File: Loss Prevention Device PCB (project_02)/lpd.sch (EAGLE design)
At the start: 5 parts, among them K1 LPPB041NGCN-RC, U2 GT-U7, U3 HM-10

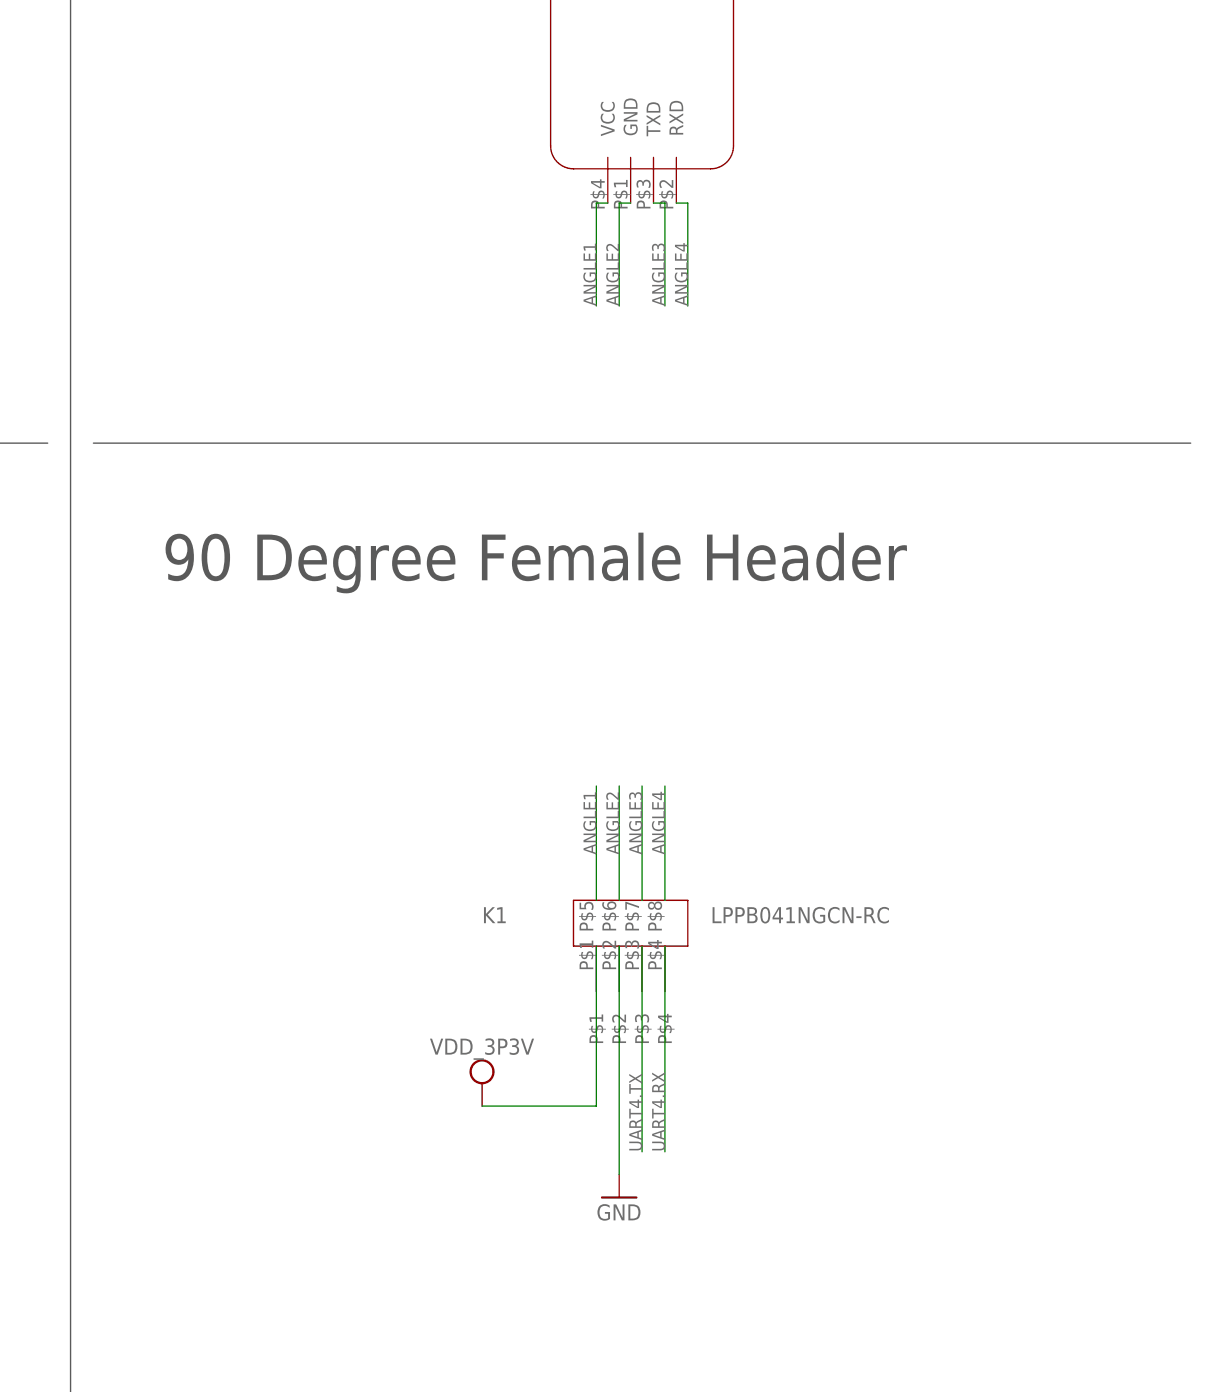
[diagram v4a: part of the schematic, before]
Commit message: Removed 90 degree header and updated footprints
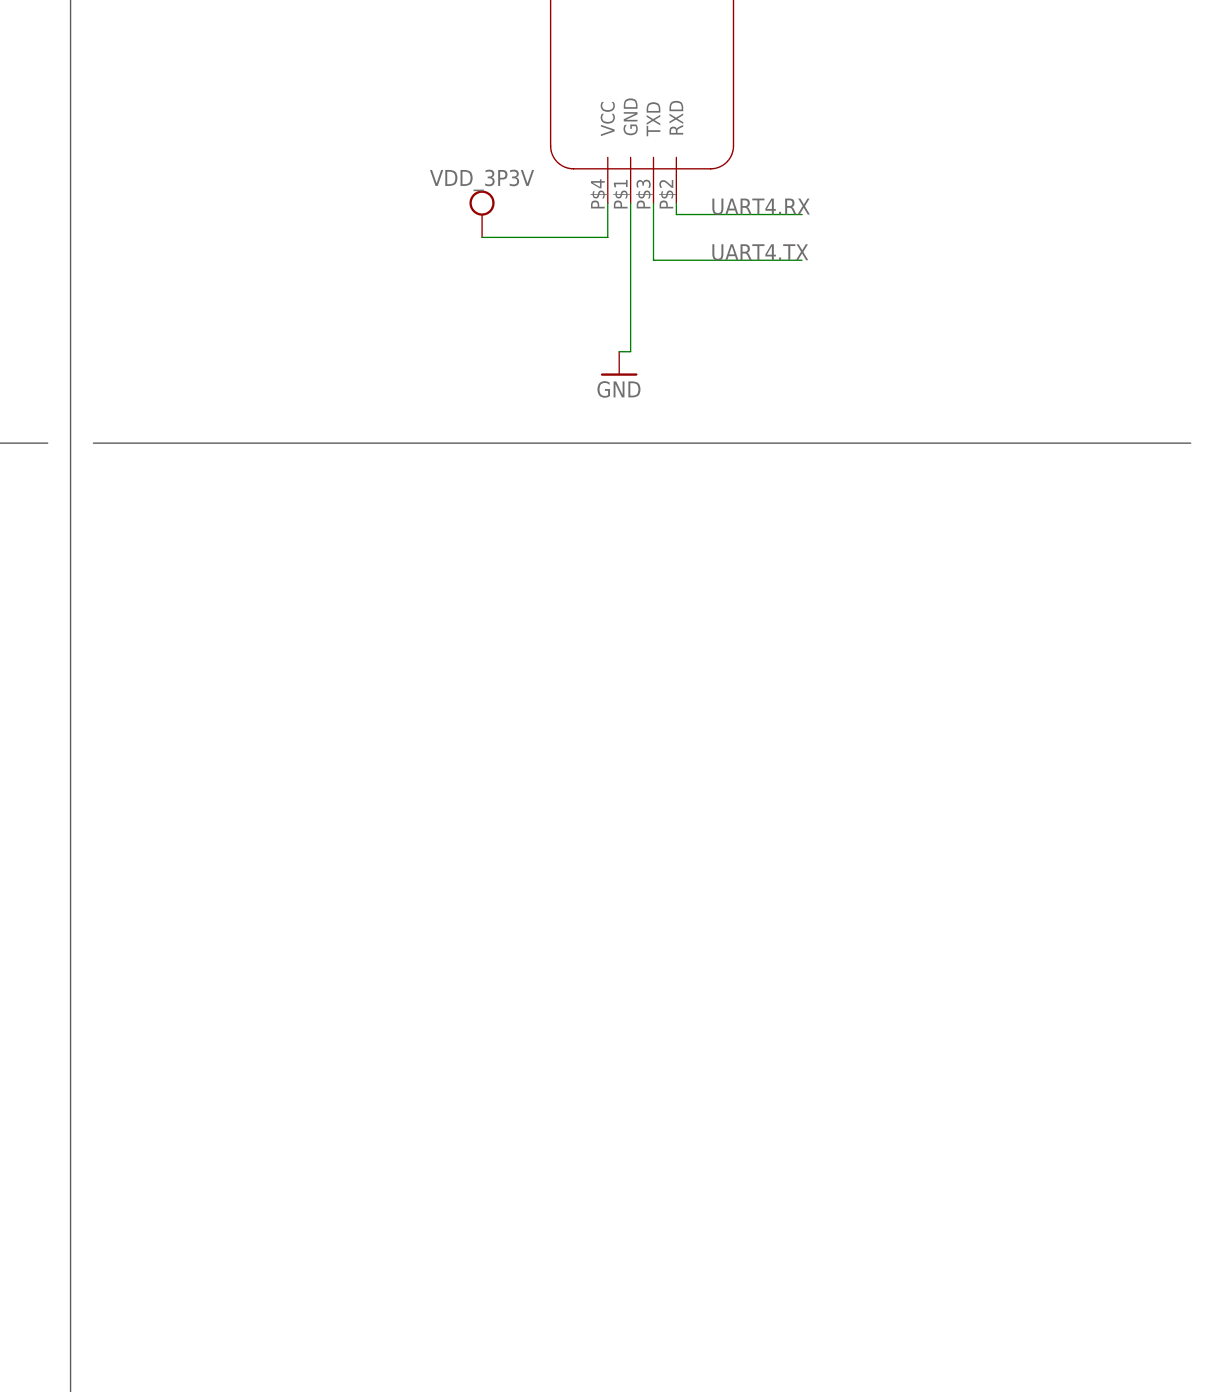
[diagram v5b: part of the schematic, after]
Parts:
- removed K1: LPPB041NGCN-RC, lpd:LPPB041NGCN-RC
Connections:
- removed net ANGLE1: K1.P$5, U3.VCC
- removed net ANGLE2: K1.P$6, U3.GND
- removed net ANGLE3: K1.P$7, U3.TXD
- removed net ANGLE4: K1.P$8, U3.RXD
- net GND: now also U3.GND; no longer K1.P$2
- net UART4.RX: now also U3.RXD; no longer K1.P$4
- net UART4.TX: now also U3.TXD; no longer K1.P$3
- net VDD_3P3V: now also U3.VCC; no longer K1.P$1
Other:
- note removed: "90 Degree Female Header"
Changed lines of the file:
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@@
 <parts>
 <part name="FRAME1" library="ENGI301" deviceset="FRAMES_A3L-LOC" device=""/>
-<part name="K1" library="lpd" deviceset="LPPB041NGCN-RC" device=""/>
 <part name="U2" library="lpd" deviceset="GT-U7" device=""/>
 <part name="X1" library="lpd" deviceset="GHI2_USB_HOST_W/CHASSIS_GND" device=""/>
@@
 <part name="SUPPLY3" library="lpd" deviceset="VDD_3P3V" device=""/>
 <part name="GND4" library="lpd" deviceset="GND" device=""/>
-<part name="GND5" library="lpd" deviceset="GND" device=""/>
-<part name="SUPPLY4" library="lpd" deviceset="VDD_3P3V" device=""/>
 <part name="SUPPLY5" library="BeagleBone_Blue" deviceset="GHI-POWERGOUNDSUPPLY_CGND" device=""/>
 <part name="SUPPLY6" library="BeagleBone_Blue" deviceset="GHI-POWERGOUNDSUPPLY_CGND" device=""/>
@@
 <part name="SUPPLY1" library="lpd" deviceset="VDD_3P3V" device=""/>
 <part name="SUPPLY2" library="lpd" deviceset="VDD_3P3V" device=""/>
+<part name="SUPPLY4" library="lpd" deviceset="VDD_3P3V" device=""/>
+<part name="GND2" library="lpd" deviceset="GND" device=""/>
 </parts>
 <sheets>
@@
 <text x="162.56" y="127" size="5.08" layer="97" font="vector">USB</text>
 <text x="266.7" y="243.84" size="5.08" layer="97" font="vector">Bluetooth Module</text>
-<text x="266.7" y="127" size="5.08" layer="97" font="vector">90 Degree Female Header</text>
 <wire x1="152.4" y1="142.24" x2="5.08" y2="142.24" width="0.1524" layer="97"/>
 </plain>
 <instances>
 <instance part="FRAME1" gate="G$1" x="-0.3937" y="-0.3683" smashed="yes"/>
-<instance part="K1" gate="G$1" x="312.42" y="86.36" smashed="yes">
-<attribute name="NAME" x="302.26" y="88.9" size="1.778" layer="95"/>
-<attribute name="VALUE" x="327.66" y="88.9" size="1.778" layer="96"/>
-</instance>
 <instance part="U2" gate="G$1" x="198.12" y="195.58" smashed="yes">
 <attribute name="NAME" x="195.58" y="226.06" size="1.778" layer="95"/>
@@
 <attribute name="VALUE" x="205.74" y="170.18" size="1.778" layer="96"/>
 </instance>
-<instance part="GND5" gate="1" x="317.5" y="58.42" smashed="yes">
-<attribute name="VALUE" x="314.96" y="55.88" size="1.778" layer="96"/>
-</instance>
-<instance part="SUPPLY4" gate="G$1" x="302.26" y="71.12" smashed="yes">
-<attribute name="VALUE" x="302.26" y="75.184" size="1.778" layer="96" align="center"/>
-</instance>
 <instance part="SUPPLY5" gate="G$1" x="175.26" y="81.28" smashed="yes">
 <attribute name="VALUE" x="175.26" y="77.724" size="1.27" layer="96" align="center"/>
@@
 <instance part="SUPPLY2" gate="G$1" x="121.92" y="198.12" smashed="yes">
 <attribute name="VALUE" x="124.46" y="202.184" size="1.778" layer="96" align="center"/>
+</instance>
+<instance part="SUPPLY4" gate="G$1" x="302.26" y="167.64" smashed="yes">
+<attribute name="VALUE" x="302.26" y="171.704" size="1.778" layer="96" align="center"/>
+</instance>
+<instance part="GND2" gate="1" x="317.5" y="149.86" smashed="yes">
+<attribute name="VALUE" x="314.96" y="147.32" size="1.778" layer="96"/>
 </instance>
 </instances>
@@
 </segment>
 <segment>
-<pinref part="K1" gate="G$1" pin="P$1"/>
-<pinref part="SUPPLY4" gate="G$1" pin="VDD_3P3V"/>
-<wire x1="314.96" y1="86.36" x2="314.96" y2="68.58" width="0.1524" layer="91"/>
-<wire x1="314.96" y1="68.58" x2="302.26" y2="68.58" width="0.1524" layer="91"/>
-</segment>
-<segment>
 <pinref part="U$1" gate="G$2" pin="3.3V@2"/>
 <wire x1="101.6" y1="190.5" x2="111.76" y2="190.5" width="0.1524" layer="91"/>
@@
 <pinref part="SUPPLY2" gate="G$1" pin="VDD_3P3V"/>
 </segment>
+<segment>
+<pinref part="U3" gate="G$1" pin="VCC"/>
+<wire x1="316.23" y1="168.91" x2="316.23" y2="165.1" width="0.1524" layer="91"/>
+<wire x1="316.23" y1="165.1" x2="302.26" y2="165.1" width="0.1524" layer="91"/>
+<pinref part="SUPPLY4" gate="G$1" pin="VDD_3P3V"/>
+</segment>
 </net>
 <net name="GND" class="0">
@@
 <pinref part="GND4" gate="1" pin="GND"/>
 <wire x1="208.28" y1="195.58" x2="208.28" y2="175.26" width="0.1524" layer="91"/>
-</segment>
-<segment>
-<pinref part="K1" gate="G$1" pin="P$2"/>
-<pinref part="GND5" gate="1" pin="GND"/>
-<wire x1="317.5" y1="86.36" x2="317.5" y2="60.96" width="0.1524" layer="91"/>
 </segment>
 <segment>
@@
 <junction x="40.64" y="195.58"/>
 </segment>
+<segment>
+<pinref part="U3" gate="G$1" pin="GND"/>
+<wire x1="318.77" y1="168.91" x2="318.77" y2="152.4" width="0.1524" layer="91"/>
+<wire x1="318.77" y1="152.4" x2="317.5" y2="152.4" width="0.1524" layer="91"/>
+<pinref part="GND2" gate="1" pin="GND"/>
+</segment>
 </net>
 <net name="UART2.RX" class="0">
@@
 <net name="UART4.TX" class="0">
 <segment>
-<pinref part="K1" gate="G$1" pin="P$3"/>
-<wire x1="320.04" y1="86.36" x2="320.04" y2="63.5" width="0.1524" layer="91"/>
-<label x="320.04" y="63.5" size="1.4224" layer="95" font="vector" rot="R90"/>
-</segment>
-<segment>
 <pinref part="U$1" gate="G$2" pin="UART4.TX"/>
 <wire x1="101.6" y1="177.8" x2="121.92" y2="177.8" width="0.1524" layer="91"/>
 <label x="114.3" y="177.8" size="1.778" layer="95"/>
 </segment>
+<segment>
+<pinref part="U3" gate="G$1" pin="TXD"/>
+<wire x1="321.31" y1="168.91" x2="321.31" y2="162.56" width="0.1524" layer="91"/>
+<wire x1="321.31" y1="162.56" x2="337.82" y2="162.56" width="0.1524" layer="91"/>
+<label x="327.66" y="162.56" size="1.778" layer="95"/>
+</segment>
 </net>
 <net name="UART4.RX" class="0">
-<segment>
-<pinref part="K1" gate="G$1" pin="P$4"/>
-<wire x1="322.58" y1="86.36" x2="322.58" y2="63.5" width="0.1524" layer="91"/>
-<label x="322.58" y="63.5" size="1.4224" layer="95" font="vector" rot="R90"/>
-</segment>
 <segment>
 <pinref part="U$1" gate="G$2" pin="UART4.RX"/>
@@
 <label x="114.3" y="175.26" size="1.778" layer="95"/>
 </segment>
+<segment>
+<pinref part="U3" gate="G$1" pin="RXD"/>
+<wire x1="323.85" y1="168.91" x2="323.85" y2="167.64" width="0.1524" layer="91"/>
+<wire x1="323.85" y1="167.64" x2="337.82" y2="167.64" width="0.1524" layer="91"/>
+<label x="327.66" y="167.64" size="1.778" layer="95"/>
+</segment>
 </net>
-<net name="ANGLE1" class="0">
-<segment>
-<pinref part="K1" gate="G$1" pin="P$5"/>
-<wire x1="314.96" y1="91.44" x2="314.96" y2="104.14" width="0.1524" layer="91"/>
-<label x="314.96" y="96.52" size="1.4224" layer="95" font="vector" rot="R90"/>
-</segment>
-<segment>
-<pinref part="U3" gate="G$1" pin="VCC"/>
-<wire x1="316.23" y1="168.91" x2="314.96" y2="168.91" width="0.1524" layer="91"/>
-<wire x1="314.96" y1="168.91" x2="314.96" y2="157.48" width="0.1524" layer="91"/>
-<label x="314.96" y="157.48" size="1.4224" layer="95" font="vector" rot="R90"/>
-</segment>
-</net>
-<net name="ANGLE2" class="0">
-<segment>
-<pinref part="K1" gate="G$1" pin="P$6"/>
-<wire x1="317.5" y1="91.44" x2="317.5" y2="104.14" width="0.1524" layer="91"/>
-<label x="317.5" y="96.52" size="1.4224" layer="95" font="vector" rot="R90"/>
-</segment>
-<segment>
-<pinref part="U3" gate="G$1" pin="GND"/>
-<wire x1="318.77" y1="168.91" x2="317.5" y2="168.91" width="0.1524" layer="91"/>
-<wire x1="317.5" y1="168.91" x2="317.5" y2="157.48" width="0.1524" layer="91"/>
-<label x="317.5" y="157.48" size="1.4224" layer="95" font="vector" rot="R90"/>
-</segment>
-</net>
-<net name="ANGLE3" class="0">
-<segment>
-<pinref part="K1" gate="G$1" pin="P$7"/>
-<wire x1="320.04" y1="91.44" x2="320.04" y2="104.14" width="0.1524" layer="91"/>
-<label x="320.04" y="96.52" size="1.4224" layer="95" font="vector" rot="R90"/>
-</segment>
-<segment>
-<pinref part="U3" gate="G$1" pin="TXD"/>
-<wire x1="321.31" y1="168.91" x2="322.58" y2="168.91" width="0.1524" layer="91"/>
-<wire x1="322.58" y1="168.91" x2="322.58" y2="157.48" width="0.1524" layer="91"/>
-<label x="322.58" y="157.48" size="1.4224" layer="95" font="vector" rot="R90"/>
-</segment>
-</net>
-<net name="ANGLE4" class="0">
-<segment>
-<pinref part="K1" gate="G$1" pin="P$8"/>
-<wire x1="322.58" y1="91.44" x2="322.58" y2="104.14" width="0.1524" layer="91"/>
-<label x="322.58" y="96.52" size="1.4224" layer="95" font="vector" rot="R90"/>
-</segment>
-<segment>
-<pinref part="U3" gate="G$1" pin="RXD"/>
-<wire x1="323.85" y1="168.91" x2="325.12" y2="168.91" width="0.1524" layer="91"/>
-<wire x1="325.12" y1="168.91" x2="325.12" y2="157.48" width="0.1524" layer="91"/>
-<label x="325.12" y="157.48" size="1.4224" layer="95" font="vector" rot="R90"/>
-</segment>
-</net>

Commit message: Routing
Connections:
- removed net CGND: X1.CG1, X1.CG2
- net GND: now also X1.CG1, X1.CG2
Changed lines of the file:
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@@
 <part name="SUPPLY3" library="lpd" deviceset="VDD_3P3V" device=""/>
 <part name="GND4" library="lpd" deviceset="GND" device=""/>
-<part name="SUPPLY5" library="BeagleBone_Blue" deviceset="GHI-POWERGOUNDSUPPLY_CGND" device=""/>
-<part name="SUPPLY6" library="BeagleBone_Blue" deviceset="GHI-POWERGOUNDSUPPLY_CGND" device=""/>
 <part name="GND3" library="lpd" deviceset="GND" device=""/>
 <part name="U$1" library="lpd" deviceset="POCKETBEAGLE" device=""/>
@@
 <part name="SUPPLY4" library="lpd" deviceset="VDD_3P3V" device=""/>
 <part name="GND2" library="lpd" deviceset="GND" device=""/>
+<part name="GND5" library="lpd" deviceset="GND" device=""/>
+<part name="GND6" library="lpd" deviceset="GND" device=""/>
 </parts>
 <sheets>
@@
 <attribute name="VALUE" x="205.74" y="170.18" size="1.778" layer="96"/>
 </instance>
-<instance part="SUPPLY5" gate="G$1" x="175.26" y="81.28" smashed="yes">
-<attribute name="VALUE" x="175.26" y="77.724" size="1.27" layer="96" align="center"/>
-</instance>
-<instance part="SUPPLY6" gate="G$1" x="228.6" y="81.28" smashed="yes">
-<attribute name="VALUE" x="228.6" y="77.724" size="1.27" layer="96" align="center"/>
-</instance>
 <instance part="GND3" gate="1" x="205.74" y="124.46" smashed="yes" rot="R180">
 <attribute name="VALUE" x="208.28" y="127" size="1.778" layer="96" rot="R180"/>
@@
 <instance part="GND2" gate="1" x="317.5" y="149.86" smashed="yes">
 <attribute name="VALUE" x="314.96" y="147.32" size="1.778" layer="96"/>
+</instance>
+<instance part="GND5" gate="1" x="175.26" y="81.28" smashed="yes">
+<attribute name="VALUE" x="172.72" y="78.74" size="1.778" layer="96"/>
+</instance>
+<instance part="GND6" gate="1" x="228.6" y="81.28" smashed="yes">
+<attribute name="VALUE" x="226.06" y="78.74" size="1.778" layer="96"/>
 </instance>
 </instances>
@@
 <pinref part="GND2" gate="1" pin="GND"/>
 </segment>
+<segment>
+<pinref part="X1" gate="G$1" pin="CG1"/>
+<wire x1="190.5" y1="86.36" x2="175.26" y2="86.36" width="0.1524" layer="91"/>
+<wire x1="175.26" y1="86.36" x2="175.26" y2="83.82" width="0.1524" layer="91"/>
+<pinref part="GND5" gate="1" pin="GND"/>
+</segment>
+<segment>
+<pinref part="X1" gate="G$1" pin="CG2"/>
+<wire x1="228.6" y1="83.82" x2="228.6" y2="86.36" width="0.1524" layer="91"/>
+<wire x1="228.6" y1="86.36" x2="213.36" y2="86.36" width="0.1524" layer="91"/>
+<pinref part="GND6" gate="1" pin="GND"/>
+</segment>
 </net>
 <net name="UART2.RX" class="0">
@@
 </segment>
 </net>
-<net name="CGND" class="0">
-<segment>
-<pinref part="X1" gate="G$1" pin="CG1"/>
-<pinref part="SUPPLY5" gate="G$1" pin="CGND"/>
-<wire x1="190.5" y1="86.36" x2="175.26" y2="86.36" width="0.1524" layer="91"/>
-<wire x1="175.26" y1="86.36" x2="175.26" y2="83.82" width="0.1524" layer="91"/>
-</segment>
-<segment>
-<pinref part="SUPPLY6" gate="G$1" pin="CGND"/>
-<pinref part="X1" gate="G$1" pin="CG2"/>
-<wire x1="228.6" y1="83.82" x2="228.6" y2="86.36" width="0.1524" layer="91"/>
-<wire x1="228.6" y1="86.36" x2="213.36" y2="86.36" width="0.1524" layer="91"/>
-</segment>
-</net>
